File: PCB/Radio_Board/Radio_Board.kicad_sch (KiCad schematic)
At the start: 1 part, among them J1 Conn_02x08_Counter_Clockwise

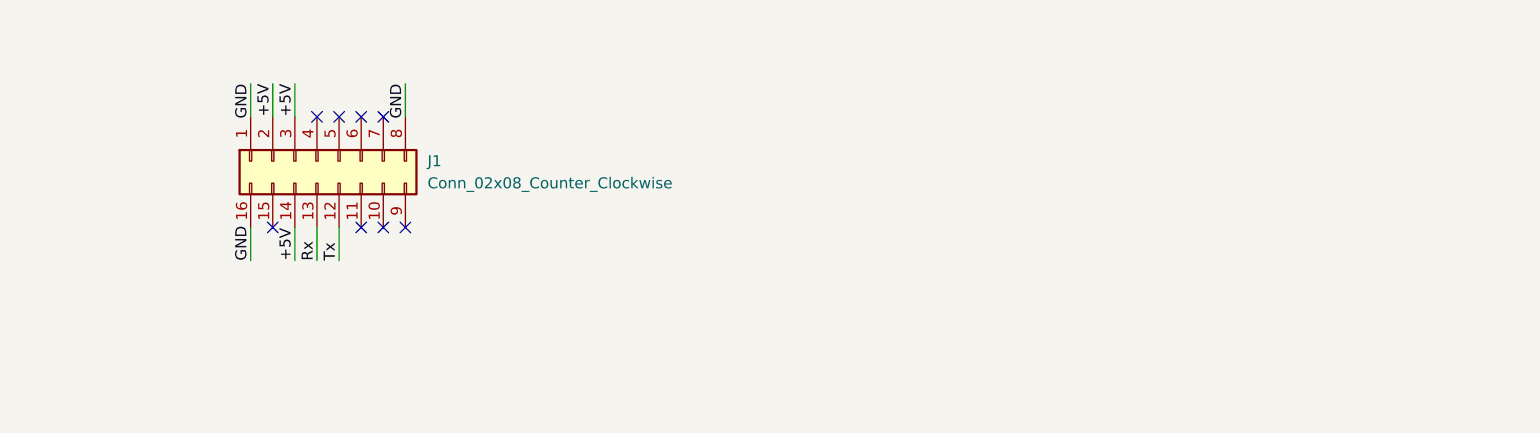
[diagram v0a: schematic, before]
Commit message: added connector and started layout
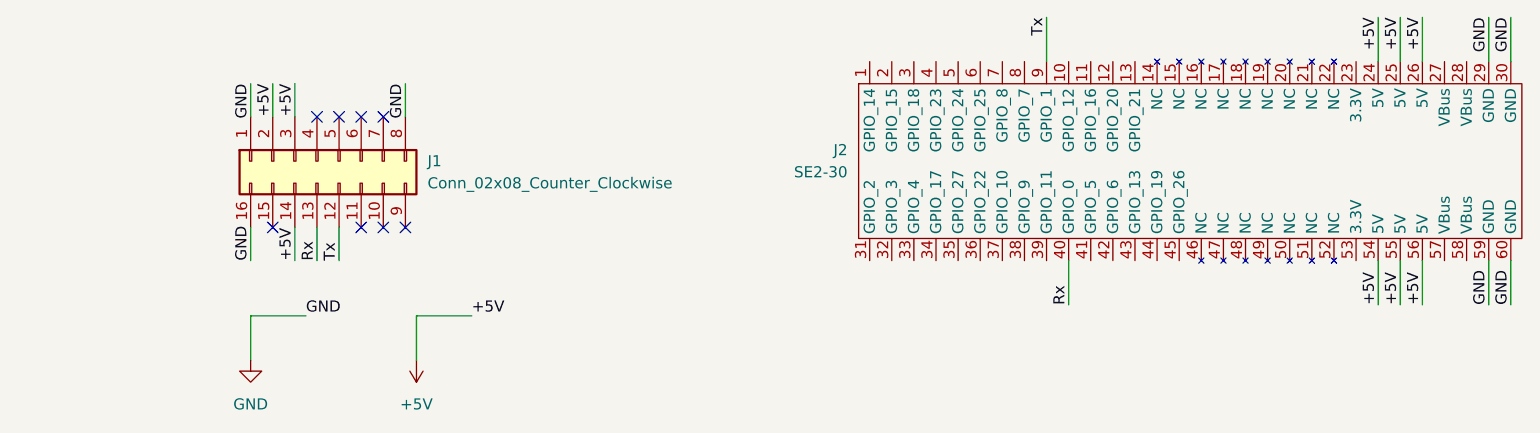
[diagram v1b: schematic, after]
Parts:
- added J2: SE2-30, SE2-30:SE2-30, symbol SE2-30:SE2-30
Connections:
- net +5V: now also J2.24 (5V), J2.25 (5V), J2.26 (5V), J2.54 (5V), J2.55 (5V), J2.56 (5V)
- net GND: now also J2.29 (GND), J2.30 (GND), J2.59 (GND), J2.60 (GND)
- net Rx: now also J2.40 (GPIO_0)
- net Tx: now also J2.9 (GPIO_1)

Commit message: Wired Layout
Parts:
- removed J1: Conn_02x08_Counter_Clockwise, Connector_PinHeader_2.54mm:PinHeader_2x08_P2.54mm_Vertical, symbol Connector_Generic:Conn_02x08_Counter_Clockwise
- added J3: Conn_02x08_Odd_Even, Connector_PinHeader_2.54mm:PinHeader_2x08_P2.54mm_Vertical, symbol Connector_Generic:Conn_02x08_Odd_Even
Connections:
- net +5V: now also J3.4 (Pin_4), J3.5 (Pin_5), J3.6 (Pin_6)
- net GND: now also J3.1 (Pin_1), J3.16 (Pin_16), J3.2 (Pin_2)
- net Rx: now also J3.7 (Pin_7)
- net Tx: now also J3.9 (Pin_9)
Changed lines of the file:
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@@
+	)
+	(symbol
+		(lib_id "Connector_Generic:Conn_02x08_Odd_Even")
+		(at 62.23 71.12 90)
+		(unit 1)
+		(exclude_from_sim no)
+		(in_bom yes)
+		(on_board yes)
+		(dnp no)
+		(fields_autoplaced yes)
+		(property "Reference" "J3"
+			(at 52.07 68.5799 90)
+			(effects
+				(font
+					(size 1.27 1.27)
+				)
+				(justify left)
+			)
+		)
+		(property "Value" "Conn_02x08_Odd_Even"
+			(at 52.07 71.1199 90)
+			(effects
+				(font
+					(size 1.27 1.27)
+				)
+				(justify left)
+			)
+		)
+		(property "Footprint" "Connector_PinHeader_2.54mm:PinHeader_2x08_P2.54mm_Vertical"
+			(at 62.23 71.12 0)
+			(effects
+				(font
+					(size 1.27 1.27)
+				)
+				(hide yes)
+			)
+		)
+		(property "Datasheet" "~"
+			(at 62.23 71.12 0)
+			(effects
+				(font
+					(size 1.27 1.27)
+				)
+				(hide yes)
+			)
+		)
+		(property "Description" "Generic connector, double row, 02x08, odd/even pin numbering scheme (row 1 odd numbers, row 2 even numbers), script generated (kicad-library-utils/schlib/autogen/connector/)"
+			(at 62.23 71.12 0)
+			(effects
+				(font
+					(size 1.27 1.27)
+				)
+				(hide yes)
+			)
+		)
+		(pin "3"
+		)
+		(pin "7"
+		)
+		(pin "16"
+		)
+		(pin "2"
+		)
+		(pin "11"
+		)
+		(pin "4"
+		)
+		(pin "12"
+		)
+		(pin "14"
+		)
+		(pin "1"
+		)
+		(pin "15"
+		)
+		(pin "13"
+		)
+		(pin "9"
+		)
+		(pin "8"
+		)
+		(pin "6"
+		)
+		(pin "10"
+		)
+		(pin "5"
+		)
+		(instances
+			(project ""
+				(path "/a413d58d-b9bf-4f0f-a8b3-75c330daf0fc"
+					(reference "J3")
+					(unit 1)
+				)
+			)
+		)
 	)
 	(symbol
@@
 					(unit 1)
 				)
-			)
-		)
-	)
-	(symbol
-		(lib_id "Connector_Generic:Conn_02x08_Counter_Clockwise")
-		(at 62.23 68.58 90)
-		(mirror x)
-		(unit 1)
-		(exclude_from_sim no)
-		(in_bom yes)
-		(on_board yes)
-		(dnp no)
-		(property "Reference" "J1"
-			(at 74.93 68.5799 90)
-			(effects
-				(font
-					(size 1.27 1.27)
-				)
-				(justify right)
-			)
-		)
-		(property "Value" "Conn_02x08_Counter_Clockwise"
-			(at 74.93 71.1199 90)
-			(effects
-				(font
-					(size 1.27 1.27)
-				)
-				(justify right)
-			)
-		)
-		(property "Footprint" "Connector_PinHeader_2.54mm:PinHeader_2x08_P2.54mm_Vertical"
-			(at 62.23 68.58 0)
-			(effects
-				(font
-					(size 1.27 1.27)
-				)
-				(hide yes)
-			)
-		)
-		(property "Datasheet" "~"
-			(at 62.23 68.58 0)
-			(effects
-				(font
-					(size 1.27 1.27)
-				)
-				(hide yes)
-			)
-		)
-		(property "Description" "Generic connector, double row, 02x08, counter clockwise pin numbering scheme (similar to DIP package numbering), script generated (kicad-library-utils/schlib/autogen/connector/)"
-			(at 62.23 68.58 0)
-			(effects
-				(font
-					(size 1.27 1.27)
-				)
-				(hide yes)
-			)
-		)
-		(pin "10"
-		)
-		(pin "15"
-		)
-		(pin "16"
-		)
-		(pin "9"
-		)
-		(pin "11"
-		)
-		(pin "2"
-		)
-		(pin "5"
-		)
-		(pin "4"
-		)
-		(pin "3"
-		)
-		(pin "1"
-		)
-		(pin "14"
-		)
-		(pin "6"
-		)
-		(pin "13"
-		)
-		(pin "12"
-		)
-		(pin "8"
-		)
-		(pin "7"
-		)
-		(instances
-			(project ""
-				(path "/a413d58d-b9bf-4f0f-a8b3-75c330daf0fc"
-					(reference "J1")
-					(unit 1)
-				)

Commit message: updated footprint from lib
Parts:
- J2: footprint SE2-30:SE2-30 -> SE2-30_Footprint:SE2-30
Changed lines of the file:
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@@
 			)
 		)
-		(property "Footprint" "SE2-30:SE2-30"
+		(property "Footprint" "SE2-30_Footprint:SE2-30"
 			(at 162.56 58.42 0)
 			(effects
